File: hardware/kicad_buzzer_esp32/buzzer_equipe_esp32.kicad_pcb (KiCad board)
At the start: 2 copper layers, 125 x 140 mm, 7 parts, among them J2 Module charge TP4056+protect+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, J3 Module vibreur IN/VCC/GND, SW1 Bouton BUZZ (fils volants), SW2 Interrupteur marche/arret (fi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, U1L ESP32 colonne gauche (broches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, U1R ESP32 colonne droite (broches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

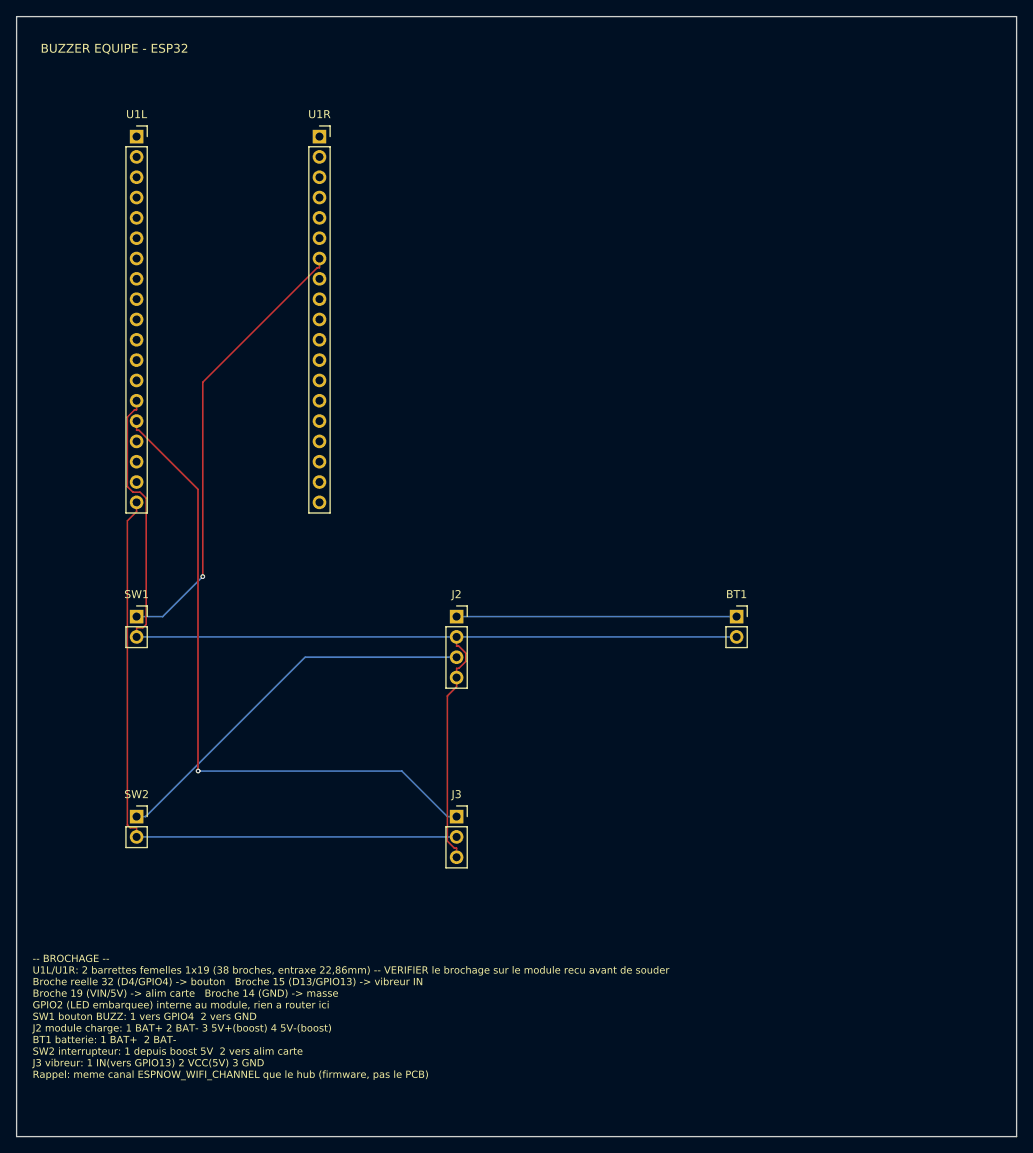
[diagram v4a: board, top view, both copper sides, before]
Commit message: hardware: cartes retrecies, guide serigraphie retire, keepout sous le nRF24
3 demandes traitees sur les 3 cartes:

- Retrait du texte-guide en serigraphie (bloc BROCHAGE) -- n'a plus sa
  place sur un circuit destine a la fabrication reelle. Repere de
  composant standard (A1L, J1, C1...) conserve, paragraphe d'instructions
  retire.
- Cartes nettement plus compactes: nano 125x145 -> 90x100mm, hub
  185x145 -> 137x85mm, esp32 130x145 -> 68x101mm.
- Nano/hub: C1/C3 (decouplage nRF24) rapproches encore plus de J1/J_NRF.
- Zone sans cuivre (keepout, pistes/vias/plans interdits sur F.Cu ET B.Cu)
  ajoutee sous l'emplacement du module nRF24 PA+LNA sur les 2 cartes qui en
  ont un (nano, hub) -- pas de cuivre sous l'antenne du module. Verifie
  reellement respecte par Freerouting (pas juste accepte par kicad-cli):
  un test dedie avec un keepout bloquant deliberement le seul chemin entre
  2 pastilles a fait router 0 piste par l'autorouteur, preuve qu'il n'etait
  pas ignore. Premiere disposition (keepout collant a J1 sur plusieurs
  cotes) a bloque le routeur (8 pistes indefiniment non routees apres 100+
  passes) -- corrige en placant le keepout en presqu'ile contre le bord de
  la carte, ne bloquant aucun chemin de routage necessaire.

Les 3 cartes re-routees (Freerouting) et revalidees (kicad-cli pcb drc):
0 violation de clearance, 0 element non connecte, 0 track_dangling sur les
3, et 0 piste a l'interieur des zones keepout (verifie par script).

Co-Authored-By: Claude Sonnet 5 <noreply@anthropic.com>
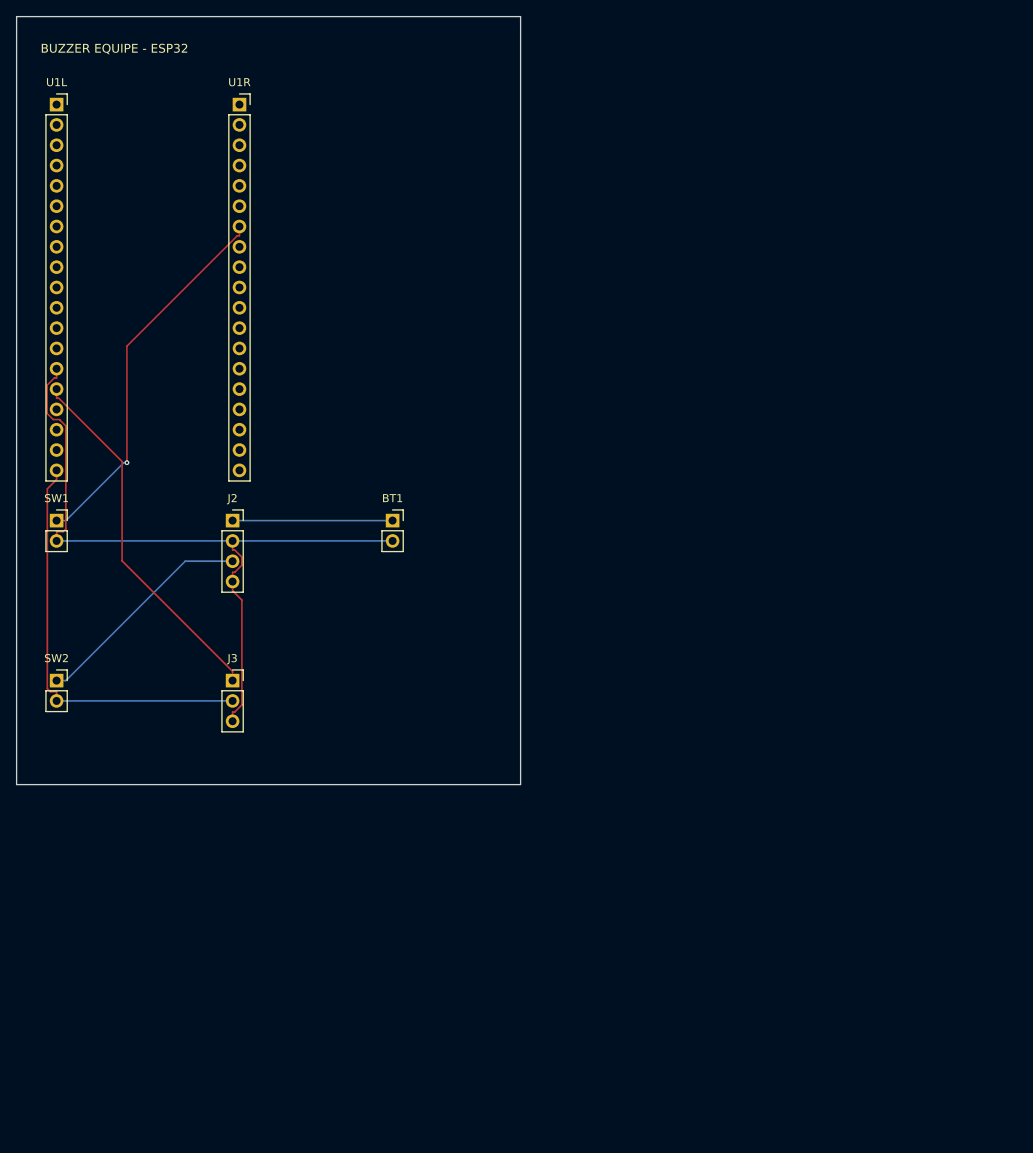
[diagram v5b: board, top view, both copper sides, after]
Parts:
- moved BT1 44.6 mm to (52.0, 68.0)
- moved J3 32.8 mm to (32.0, 88.0)
- moved J2 30.5 mm to (32.0, 68.0)
- moved SW2 19.7 mm to (10.0, 88.0)
- moved SW1 15.6 mm to (10.0, 68.0)
- moved U1L 10.8 mm to (10.0, 16.0)
- moved U1R 10.8 mm to (32.9, 16.0)
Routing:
- net GND: track 137.6 -> 91.5 mm
- net VIBE_IN: track 81.8 -> 45.7 mm, vias 1 -> 0
- net VCC_5V_SW: track 83.3 -> 52.2 mm
- net VCC_5V_RAW: track 48.3 -> 28.2 mm
- net BAT_PLUS: track 35.0 -> 20.0 mm
- net BTN_SIG: track 56.3 -> 47.3 mm
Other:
- board size 125 x 140 mm -> 63 x 96 mm
- board text removed: "-- BROCHAGE -- U1L/U1R: 2 barrettes femelles 1x19 (38 broches, entraxe 22,86mm) -- VERIFIER le brochage sur le module recu avant de souder Broche reelle 32 (D4/GPIO4) -> bouton Broche 15 (D13/GPIO13) -> vibreur IN Broche 19 (VIN/5V) -> alim carte Broche 14 (GND) -> masse GPIO2 (LED embarquee) interne au module, rien a router ici SW1 bouton BUZZ: 1 vers GPIO4 2 vers GND J2 module charge: 1 BAT+ 2 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"

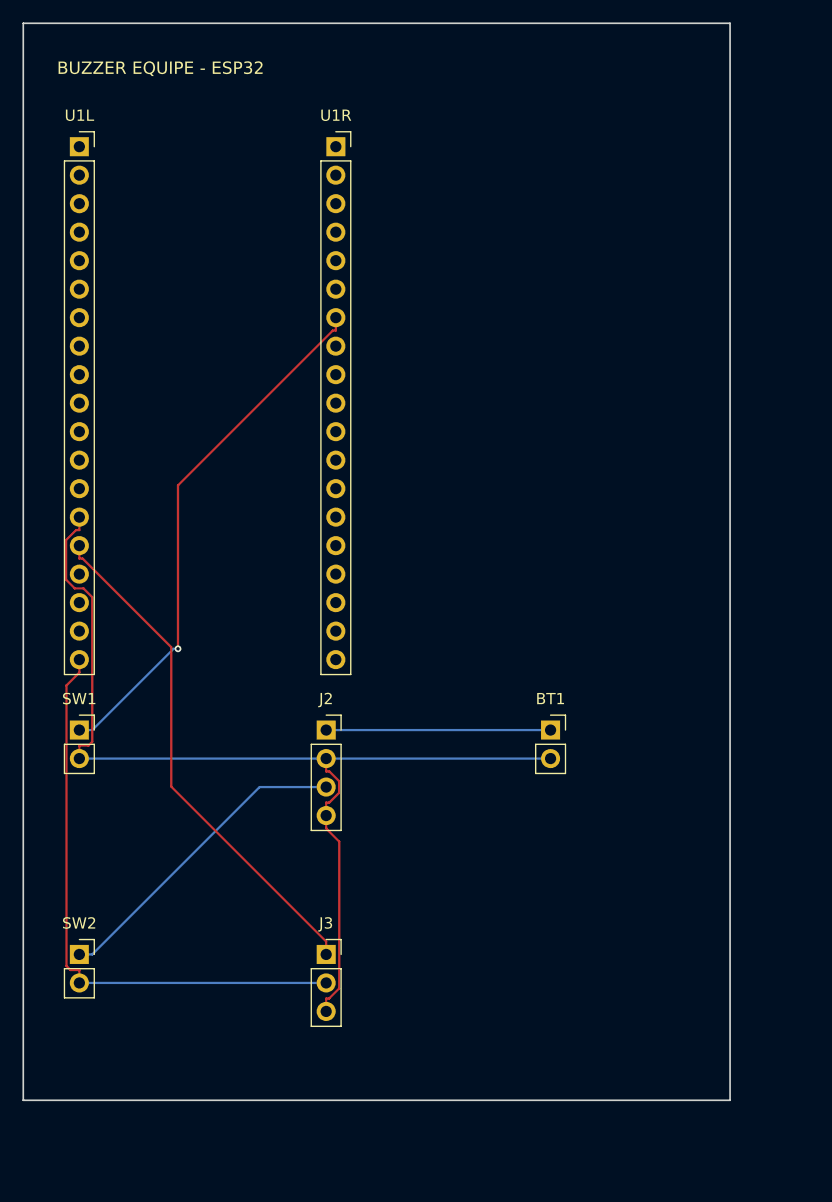
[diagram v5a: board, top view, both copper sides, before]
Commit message: hardware: passifs + petits connecteurs en CMS pour assemblage PCBA
Par choix explicite (assemblage machine chez le fabricant plutot que
soudure manuelle): resistances et condensateurs passent en CMS 0805
(R_0805/C_0805), et les petits connecteurs "fils volants" (bouton, module
de charge, module vibreur, batterie, interrupteur) passent en variantes
SMD des memes footprints PinSocket. Meme numerotation de broche que les
versions traversantes -- NETS inchange, seule l'empreinte change.

Restent traversants (headers de modules enfichables, pas adaptes au CMS):
A1L/A1R (nano), U1L/U1R (esp32), U_ESP32L/R (hub), J1/J_NRF (nRF24),
J_MEGA (hub).

Nano: C1, SW1, SW2, J2, J3, BT1 -> CMS.
ESP32: SW1, SW2, J2, J3, BT1 -> CMS.
Hub: R1-R4, C1-C3 -> CMS.

Les 3 cartes re-routees (Freerouting) et revalidees (kicad-cli pcb drc):
0 violation de clearance, 0 element non connecte, keepout nRF24 toujours
respecte (0 piste dedans, verifie par script), 0 track_dangling apres
nettoyage des residus d'autorouter habituels.

Co-Authored-By: Claude Sonnet 5 <noreply@anthropic.com>
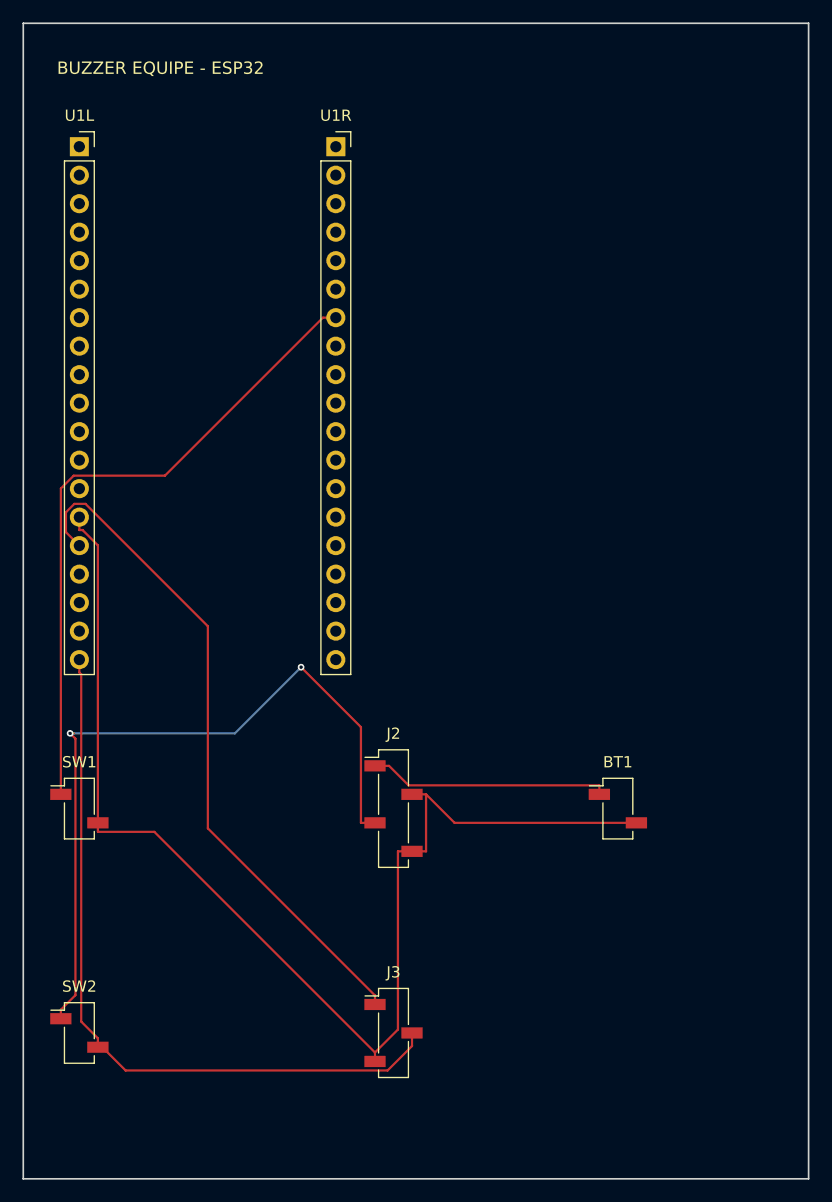
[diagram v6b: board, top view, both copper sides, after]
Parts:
- BT1: value Batterie LiPo 1S 1000-1200mAh (cablee/soudee) -> Batterie LiPo 1S 1000-1200mAh (cablee/soudee) - CMS; footprint Connector_PinSocket_2.54mm:PinSocket_1x02_P2.54mm_Vertical -> Connector_PinSocket_2.54mm:PinSocket_1x02_P2.54mm_Vertical_SMD_Pin1Left
- J2: value Module charge TP4056+protect+boost USB-C -> Module charge TP4056+protect+boost USB-C - CMS; footprint Connector_PinSocket_2.54mm:PinSocket_1x04_P2.54mm_Vertical -> Connector_PinSocket_2.54mm:PinSocket_1x04_P2.54mm_Vertical_SMD_Pin1Left
- J3: value Module vibreur IN/VCC/GND -> Module vibreur IN/VCC/GND - CMS; footprint Connector_PinSocket_2.54mm:PinSocket_1x03_P2.54mm_Vertical -> Connector_PinSocket_2.54mm:PinSocket_1x03_P2.54mm_Vertical_SMD_Pin1Left
- SW1: value Bouton BUZZ (fils volants) -> Bouton BUZZ (fils volants) - CMS; footprint Connector_PinSocket_2.54mm:PinSocket_1x02_P2.54mm_Vertical -> Connector_PinSocket_2.54mm:PinSocket_1x02_P2.54mm_Vertical_SMD_Pin1Left
- SW2: value Interrupteur marche/arret (fils volants) -> Interrupteur marche/arret (fils volants) - CMS; footprint Connector_PinSocket_2.54mm:PinSocket_1x02_P2.54mm_Vertical -> Connector_PinSocket_2.54mm:PinSocket_1x02_P2.54mm_Vertical_SMD_Pin1Left
- moved BT1 9.22 mm to (58.0, 75.0)
- moved J2 9.22 mm to (38.0, 75.0)
- moved J3 9.22 mm to (38.0, 95.0)
- moved SW1 7.00 mm to (10.0, 75.0)
- moved SW2 7.00 mm to (10.0, 95.0)
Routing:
- net VCC_5V_RAW: track 28.2 -> 67.3 mm, vias 0 -> 2
- net GND: track 91.5 -> 110.0 mm
- net VIBE_IN: track 45.7 -> 60.8 mm
- net VCC_5V_SW: track 52.2 -> 66.3 mm
- net BTN_SIG: track 47.3 -> 58.1 mm, vias 1 -> 0
- net BAT_PLUS: track 20.0 -> 21.5 mm
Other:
- board size 63 x 96 mm -> 70 x 103 mm

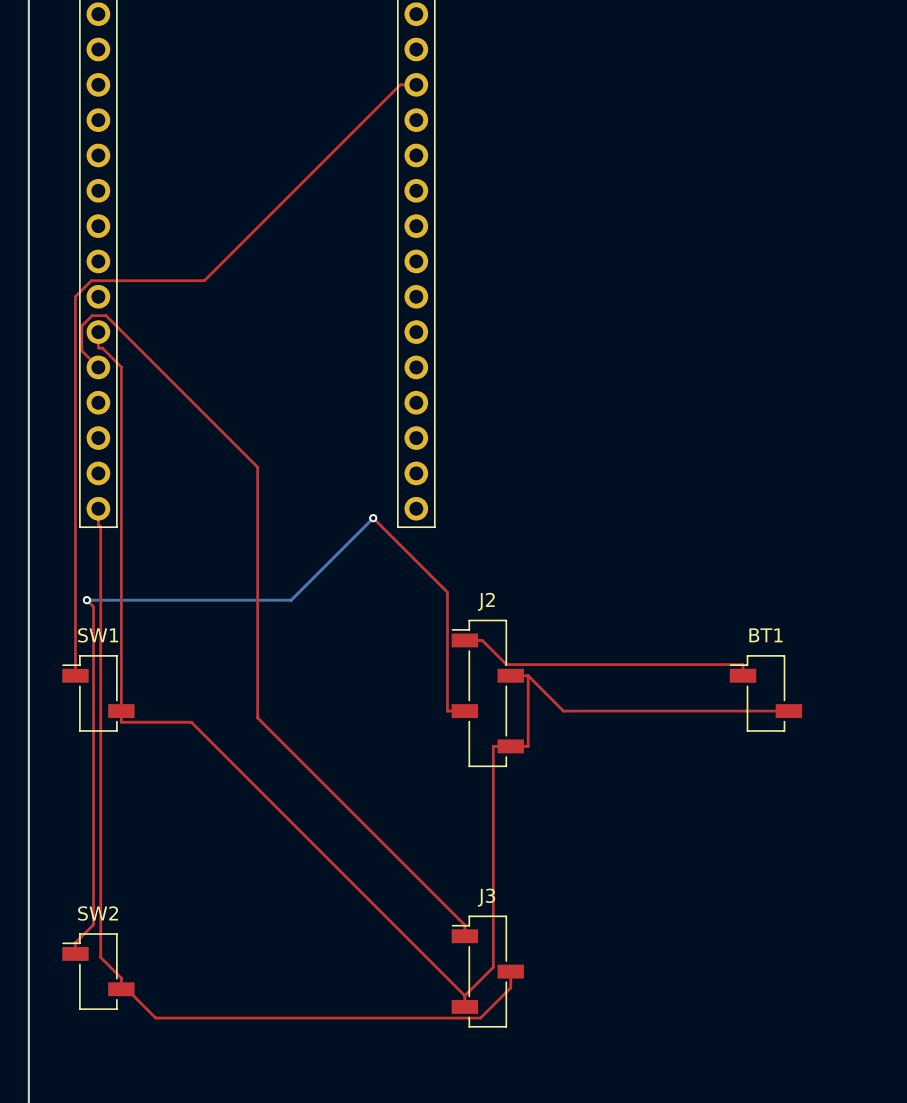
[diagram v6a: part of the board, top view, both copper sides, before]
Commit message: hardware: BT1 en vrai connecteur JST-PH (pas de simples pastilles)
Repond a "comment on va s'y prendre pour connecter le systeme de charge":
les batteries LiPo standards arrivent avec une prise JST-PH FEMELLE deja
sertie sur leurs fils -- BT1 portait jusqu'ici de simples pastilles
(recemment passees en CMS), ce qui aurait oblige a couper la prise
d'origine pour souder des fils nus. Remplace par le vrai connecteur MALE
correspondant (JST_PH_B2B-PH-K), deja recommande dans le BOM
(docs/BOM_BUZZER_EQUIPE.md: "Connecteur batterie JST-PH 2 points") mais
jamais implemente comme tel sur le PCB.

Volontairement laisse TRAVERSANT (pas de variante CMS) contrairement aux
autres petits connecteurs convertis juste avant : ce connecteur encaisse
des cycles repetes de branchement/debranchement, un maintien mecanique
qu'un pad CMS n'offre pas.

Broche 1 = + (fil rouge), broche 2 = - (fil noir), convention quasi
universelle sur les batteries LiPo JST-PH -- a verifier sur la batterie
reellement recue.

Nano et ESP32 re-routes (Freerouting) et revalides (kicad-cli pcb drc):
0 violation de clearance, 0 element non connecte, keepout nRF24 (nano)
toujours respecte, 0 track_dangling apres nettoyage des residus habituels.

Co-Authored-By: Claude Sonnet 5 <noreply@anthropic.com>
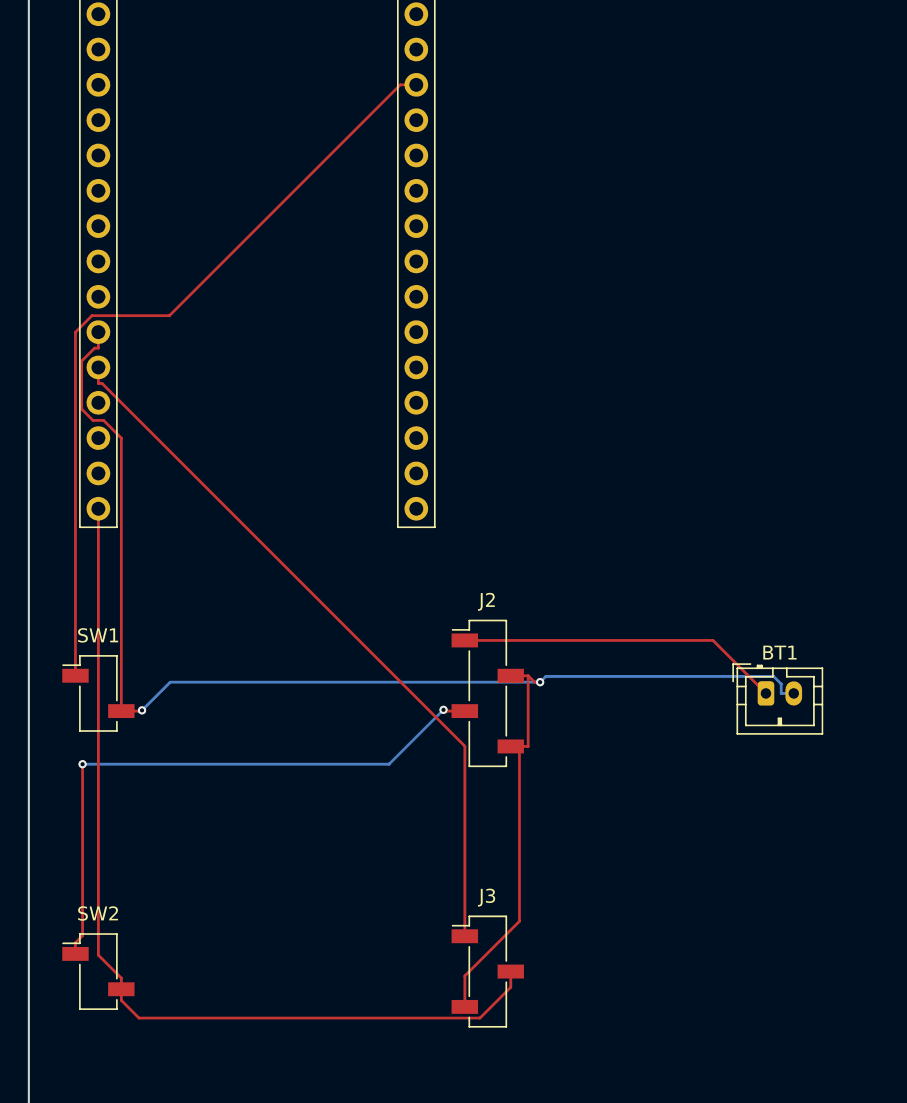
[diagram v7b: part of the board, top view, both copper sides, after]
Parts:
- BT1: value Batterie LiPo 1S 1000-1200mAh (cablee/soudee) - CMS -> Batterie LiPo 1S 1000-1200mAh - connecteur JST-PH (1=+ 2=-); footprint Connector_PinSocket_2.54mm:PinSocket_1x02_P2.54mm_Vertical_SMD_Pin1Left -> Connector_JST:JST_PH_B2B-PH-K_1x02_P2.00mm_Vertical
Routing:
- net VCC_5V_RAW: track 67.3 -> 43.1 mm
- net VIBE_IN: track 60.8 -> 52.0 mm
- net BAT_PLUS: track 21.5 -> 23.2 mm
- net BTN_SIG: track 58.1 -> 56.6 mm
- net GND: track 110.0 -> 108.8 mm, vias 0 -> 2
